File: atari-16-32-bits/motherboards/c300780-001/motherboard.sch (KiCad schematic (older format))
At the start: 0 parts

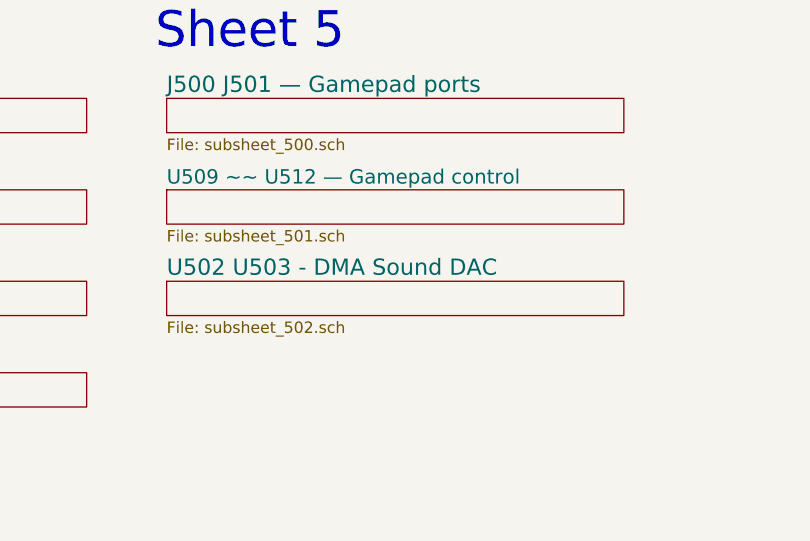
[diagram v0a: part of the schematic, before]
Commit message: split dma sound in 3 subsheet, done subsheet_502 : dma sound to dac
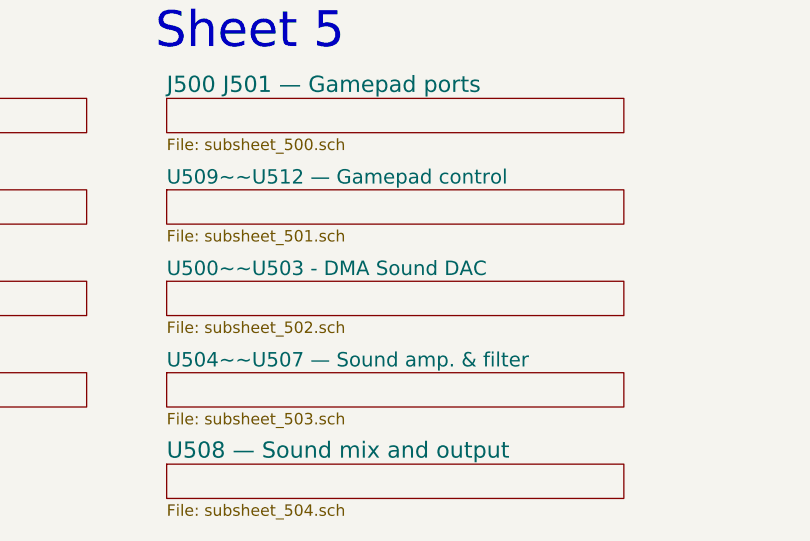
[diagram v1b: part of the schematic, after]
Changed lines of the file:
@@
 $Descr A4 8268 11693 portrait
 encoding utf-8
-Sheet 1 25
+Sheet 1 27
 Title "Converted schematics of Atari STE"
 Date ""
@@
 S 3150 5300 2000 150
 U 60C60FDB
-F0 "U509 ~~ U512 — Gamepad control" 63
+F0 "U509~~U512 — Gamepad control" 63
 F1 "subsheet_501.sch" 50
 $EndSheet
@@
 S 3150 5700 2000 150
 U 60C95DE8
-F0 "U502 U503 - DMA Sound DAC" 71
+F0 "U500~~U503 - DMA Sound DAC" 63
 F1 "subsheet_502.sch" 50
 $EndSheet
+$Sheet
+S 3150 6100 2000 150
+U 60CC3B10
+F0 "U504~~U507 — Sound amp. & filter" 63
+F1 "subsheet_503.sch" 50
+$EndSheet
+$Sheet
+S 3150 6500 2000 150
+U 60CD36E9
+F0 "U508 — Sound mix and output" 71
+F1 "subsheet_504.sch" 50
+$EndSheet
 $EndSCHEMATC

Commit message: done subsheet_600 : RAM
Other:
- note added: "Sheet 6"
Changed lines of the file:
@@
 $Descr A4 8268 11693 portrait
 encoding utf-8
-Sheet 1 27
+Sheet 1 28
 Title "Converted schematics of Atari STE"
 Date ""
@@
 F1 "subsheet_504.sch" 50
 $EndSheet
+Text Notes 5500 4700 0    157  ~ 0
+Sheet 6
+$Sheet
+S 5500 4900 2000 150
+U 60CE6C60
+F0 "U600~~U603 – RAM modules" 71
+F1 "subsheet_600.sch" 50
+$EndSheet
 $EndSCHEMATC
